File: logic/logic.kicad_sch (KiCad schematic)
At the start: 32 parts, among them J1 DIN41612_03x32_ABC, J2 Conn_02x05_Odd_Even, J3 Conn_02x05_Odd_Even, J5 Conn_02x02_Odd_Even, U1 TPIC6595, U11 LM7805_TO220, U2 TPIC6595, U3 TPIC6595, U4 TPIC6595, U5 TPIC6595, U6 TPIC6595, U7 TPIC6595, U8 TPIC6595, U9 74HC14

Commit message: Commit older work
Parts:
- removed J5: Conn_02x02_Odd_Even, symbol Connector_Generic:Conn_02x02_Odd_Even
- added J4: Conn_02x05_Odd_Even, Connector_PinHeader_2.54mm:PinHeader_2x05_P2.54mm_Vertical, symbol Connector_Generic:Conn_02x05_Odd_Even
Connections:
- net GND: now also J4.1 (Pin_1), J4.3 (Pin_3), J4.5 (Pin_5), J4.7 (Pin_7), J4.9 (Pin_9)
- net at C12.1, U11.1 (VI): now also J4.10 (Pin_10), J4.2 (Pin_2), J4.4 (Pin_4), J4.6 (Pin_6), J4.8 (Pin_8)
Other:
- note added: "J4 UNREG 6.5 - 9V IN"
- note removed: "J5-2, J5-4 UNREG 9V IN"

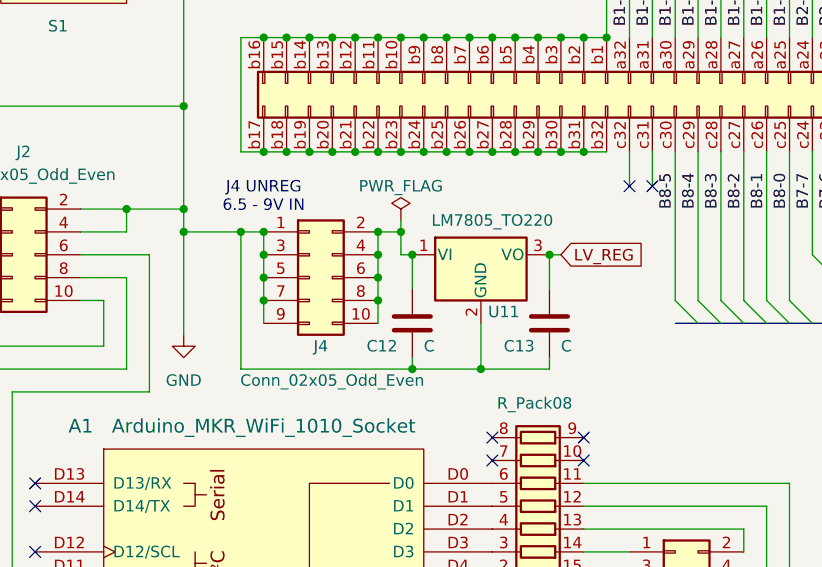
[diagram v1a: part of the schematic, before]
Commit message: Update libraries, schematic, and layout with buck converter
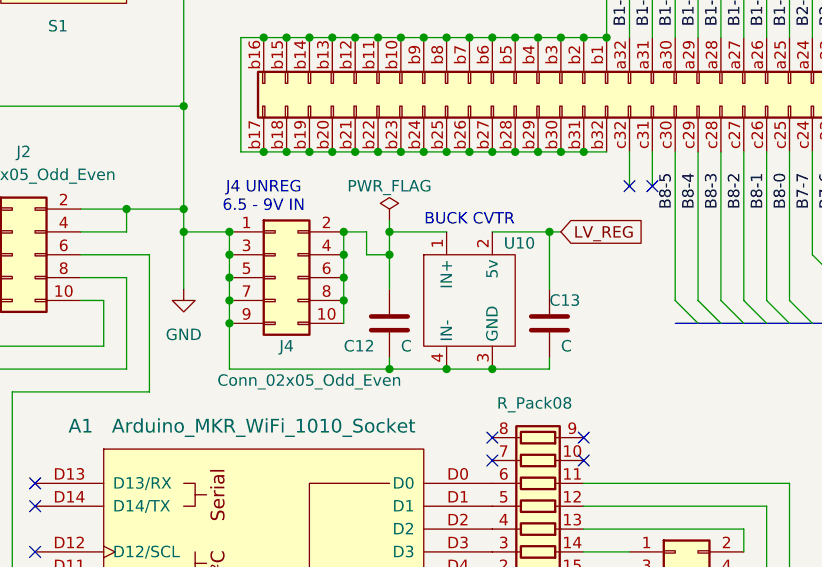
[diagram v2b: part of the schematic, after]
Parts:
- removed U11: LM7805_TO220, Package_TO_SOT_THT:TO-220-3_Vertical, symbol Regulator_Linear:LM7805_TO220
- added U10: ~, NixComp:TR4R7, symbol NixComp:TR4R7
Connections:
- net GND: now also U10.3 (GND), U10.4 (IN-)
- net LV_REG: now also U10.2 (5v)
- net at C12.1, J4.10 (Pin_10), J4.2 (Pin_2)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: now also U10.1 (IN+)
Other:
- note added: "BUCK CVTR"
- moved on the sheet: C12, J4

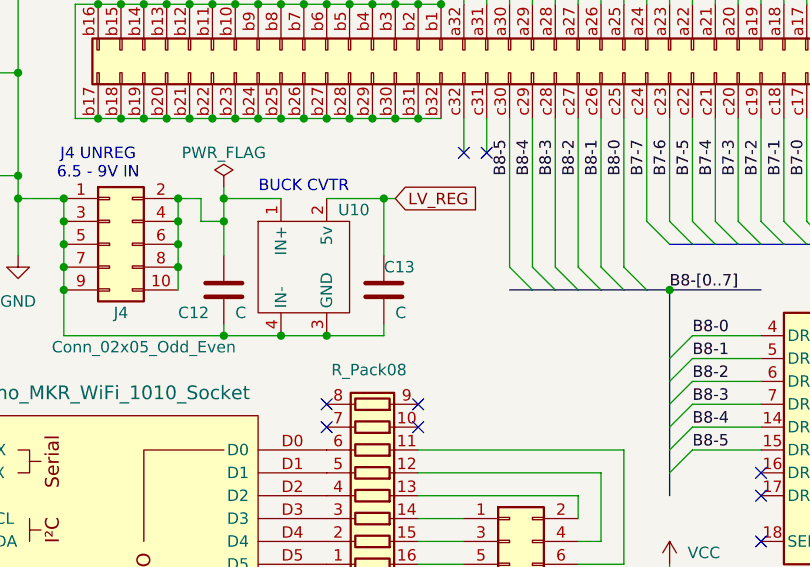
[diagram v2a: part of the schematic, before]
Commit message: Ongoing development of prototype, symbols, footprints, and logic schematic
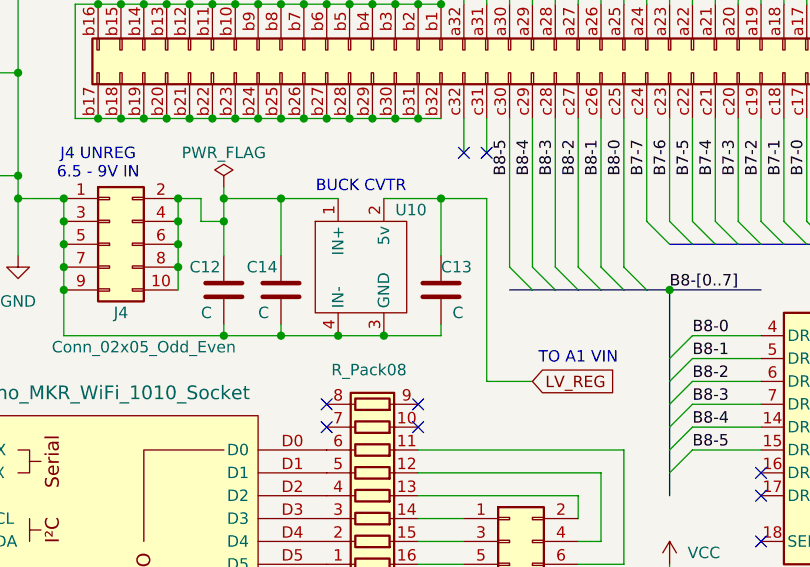
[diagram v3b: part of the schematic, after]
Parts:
- added C14: C, Capacitor_THT:C_Disc_D3.4mm_W2.1mm_P2.50mm, symbol Device:C
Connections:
- net GND: now also C14.2
- net at C12.1, J4.10 (Pin_10), J4.2 (Pin_2)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: now also C14.1
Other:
- note added: "TO A1 VIN"
- moved on the sheet: C13, U10

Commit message: Begin incorporating feedback from prototype. Checkpoint.
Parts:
- removed C1, C10, C12, C13, C14, C2, C3, C4, C5, C6, C7, C8, C9: C, Capacitor_THT:C_Disc_D3.4mm_W2.1mm_P2.50mm, symbol Device:C
- removed C11: C, Capacitor_THT:CP_Radial_D8.0mm_P2.50mm, symbol Device:C
- removed J4: Conn_02x05_Odd_Even, Connector_PinHeader_2.54mm:PinHeader_2x05_P2.54mm_Vertical, symbol Connector_Generic:Conn_02x05_Odd_Even
- removed R1: R, Resistor_THT:R_Axial_DIN0207_L6.3mm_D2.5mm_P10.16mm_Horizontal, symbol Device:R
- removed S1: ~, NixComp:NCH8200HV, symbol NixComp:NCH8200HV_170v
- removed U10: ~, NixComp:TR4R7, symbol NixComp:TR4R7
- removed U9: 74HC14, Package_DIP:DIP-14_W7.62mm_Socket, symbol 74xx:74HC14
- added U9: 74LS244, symbol 74xx:74LS244
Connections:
- net B1-0: no longer J1.a32 (Pin_a32)
- net B1-1: no longer J1.a31 (Pin_a31)
- net B1-2: no longer J1.a30 (Pin_a30)
- net B1-3: no longer J1.a29 (Pin_a29)
- net B1-4: no longer J1.a28 (Pin_a28)
- net B1-5: no longer J1.a27 (Pin_a27)
- net B1-6: no longer J1.a26 (Pin_a26)
- net B1-7: no longer J1.a25 (Pin_a25)
- net B2-0: no longer J1.a24 (Pin_a24)
- net B2-1: no longer J1.a23 (Pin_a23)
- net B2-2: no longer J1.a22 (Pin_a22)
- net B2-3: no longer J1.a21 (Pin_a21)
- net B2-4: no longer J1.a20 (Pin_a20)
- net B2-5: no longer J1.a19 (Pin_a19)
- net B2-6: no longer J1.a18 (Pin_a18)
- net B2-7: no longer J1.a17 (Pin_a17)
- net B3-0: no longer J1.a16 (Pin_a16)
- net B3-1: no longer J1.a15 (Pin_a15)
- net B3-2: no longer J1.a14 (Pin_a14)
- net B3-3: no longer J1.a13 (Pin_a13)
- net B3-4: no longer J1.a12 (Pin_a12)
- net B3-5: no longer J1.a11 (Pin_a11)
- net B3-6: no longer J1.a10 (Pin_a10)
- net B3-7: no longer J1.a9 (Pin_a9)
- net B4-0: no longer J1.a8 (Pin_a8)
- net B4-1: no longer J1.a7 (Pin_a7)
- net B4-2: no longer J1.a6 (Pin_a6)
- net B4-3: no longer J1.a5 (Pin_a5)
- net B4-4: no longer J1.a4 (Pin_a4)
- net B4-5: no longer J1.a3 (Pin_a3)
- net B5-0: no longer J1.c1 (Pin_c1)
- net B5-1: no longer J1.c2 (Pin_c2)
- net B5-2: no longer J1.c3 (Pin_c3)
- net B5-3: no longer J1.c4 (Pin_c4)
- net B5-4: no longer J1.c5 (Pin_c5)
- net B5-5: no longer J1.c6 (Pin_c6)
- net B5-6: no longer J1.c7 (Pin_c7)
- net B5-7: no longer J1.c8 (Pin_c8)
- net B6-0: no longer J1.c9 (Pin_c9)
- net B6-1: no longer J1.c10 (Pin_c10)
- net B6-2: no longer J1.c11 (Pin_c11)
- net B6-3: no longer J1.c12 (Pin_c12)
- net B6-4: no longer J1.c13 (Pin_c13)
- net B6-5: no longer J1.c14 (Pin_c14)
- net B6-6: no longer J1.c15 (Pin_c15)
- net B6-7: no longer J1.c16 (Pin_c16)
- net B7-0: no longer J1.c17 (Pin_c17)
- net B7-1: no longer J1.c18 (Pin_c18)
- net B7-2: no longer J1.c19 (Pin_c19)
- net B7-3: no longer J1.c20 (Pin_c20)
- net B7-4: no longer J1.c21 (Pin_c21)
- net B7-5: no longer J1.c22 (Pin_c22)
- net B7-6: no longer J1.c23 (Pin_c23)
- net B7-7: no longer J1.c24 (Pin_c24)
- net B8-0: no longer J1.c25 (Pin_c25)
- net B8-1: no longer J1.c26 (Pin_c26)
- net B8-2: no longer J1.c27 (Pin_c27)
- net B8-3: no longer J1.c28 (Pin_c28)
- net B8-4: no longer J1.c29 (Pin_c29)
- net B8-5: no longer J1.c30 (Pin_c30)
- net GND: no longer A1.GND, J3.7 (Pin_7), J3.9 (Pin_9)
- net HV_REG: now reaches J1.b1 (Pin_b1), J1.b10 (Pin_b10), J1.b11 (Pin_b11), J1.b12 (Pin_b12), J1.b13 (Pin_b13), J1.b14 (Pin_b14), J1.b15 (Pin_b15), J1.b16 (Pin_b16), J1.b17 (Pin_b17), J1.b18 (Pin_b18), J1.b19 (Pin_b19), J1.b2 (Pin_b2), J1.b20 (Pin_b20), J1.b21 (Pin_b21), J1.b22 (Pin_b22), J1.b23 (Pin_b23), J1.b24 (Pin_b24), J1.b25 (Pin_b25), J1.b26 (Pin_b26), J1.b27 (Pin_b27), J1.b28 (Pin_b28), J1.b29 (Pin_b29), J1.b3 (Pin_b3), J1.b30 (Pin_b30), J1.b31 (Pin_b31), J1.b32 (Pin_b32), J1.b4 (Pin_b4), J1.b5 (Pin_b5), J1.b6 (Pin_b6), J1.b7 (Pin_b7), J1.b8 (Pin_b8), J1.b9 (Pin_b9)
- new net: A1.GND, J3.7 (Pin_7), J3.9 (Pin_9)
- no-connect marks 26 -> 23
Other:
- added sheet Logic-overflow (Logic-overflow.kicad_sch)
- note removed: "BUCK CVTR"
- note removed: "DECOUPLING"
- note removed: "J4 UNREG 6.5 - 9V IN"
- note removed: "NCH8200HV 5VDC 170V"
- note removed: "UNUSED GATES"
- moved on the sheet: J1

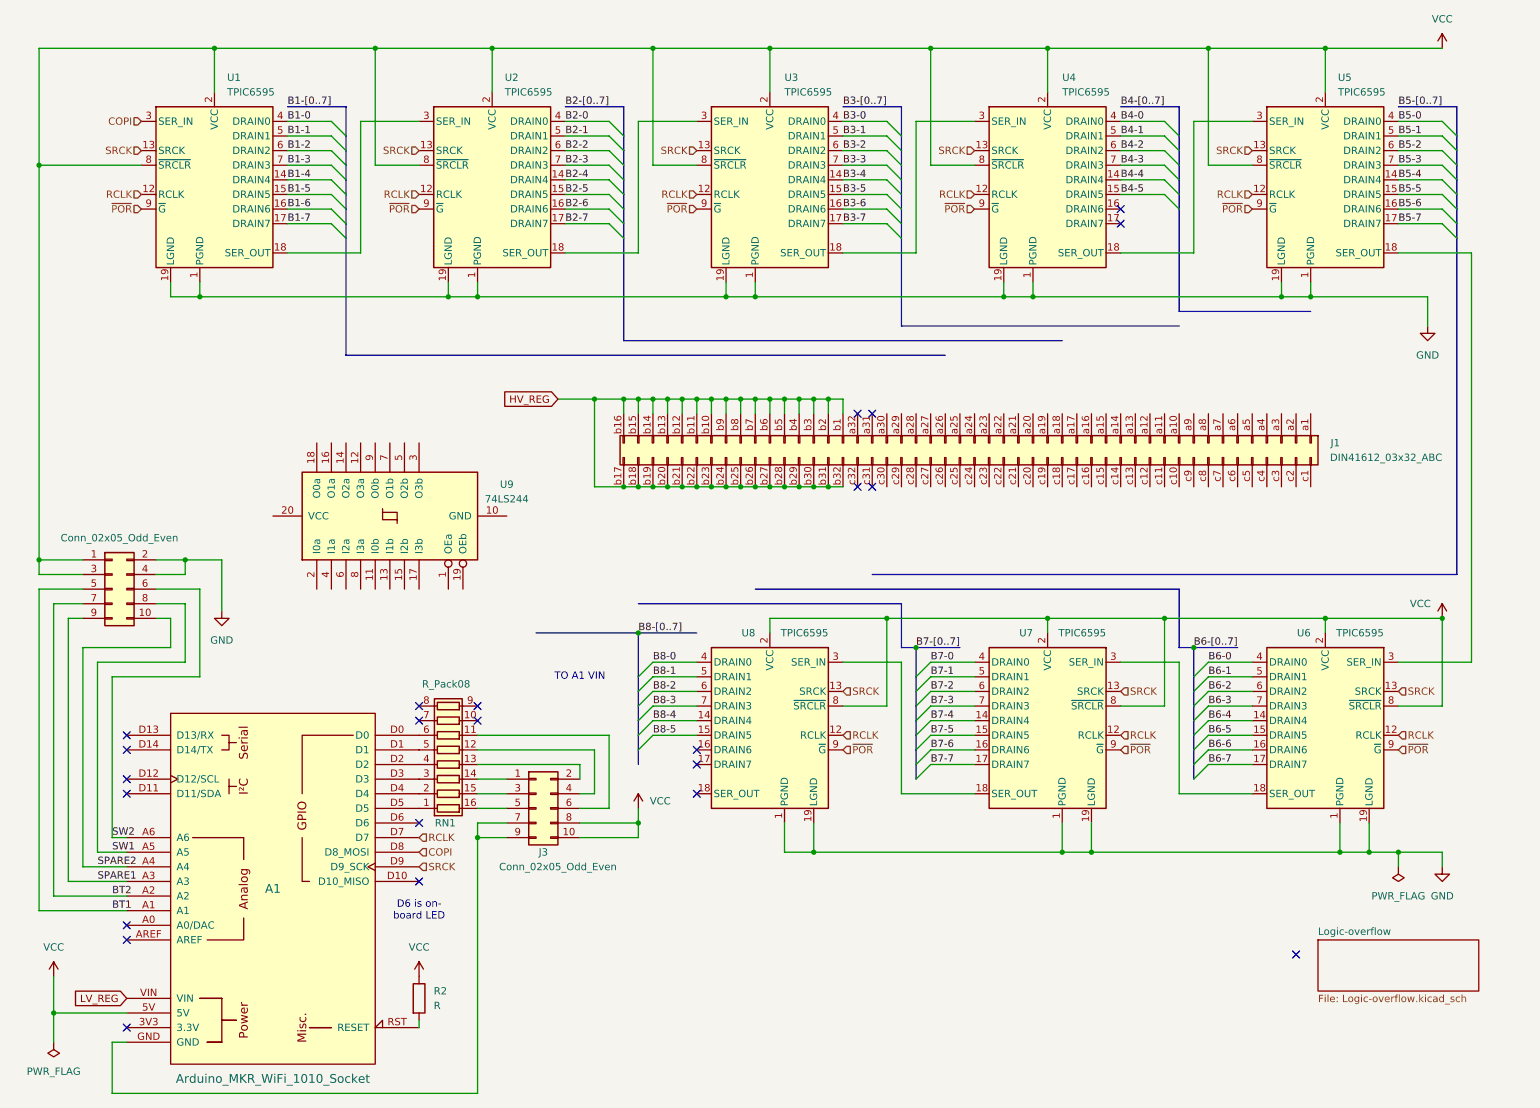
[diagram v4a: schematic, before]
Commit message: Complete schematic and begin logic board layout.
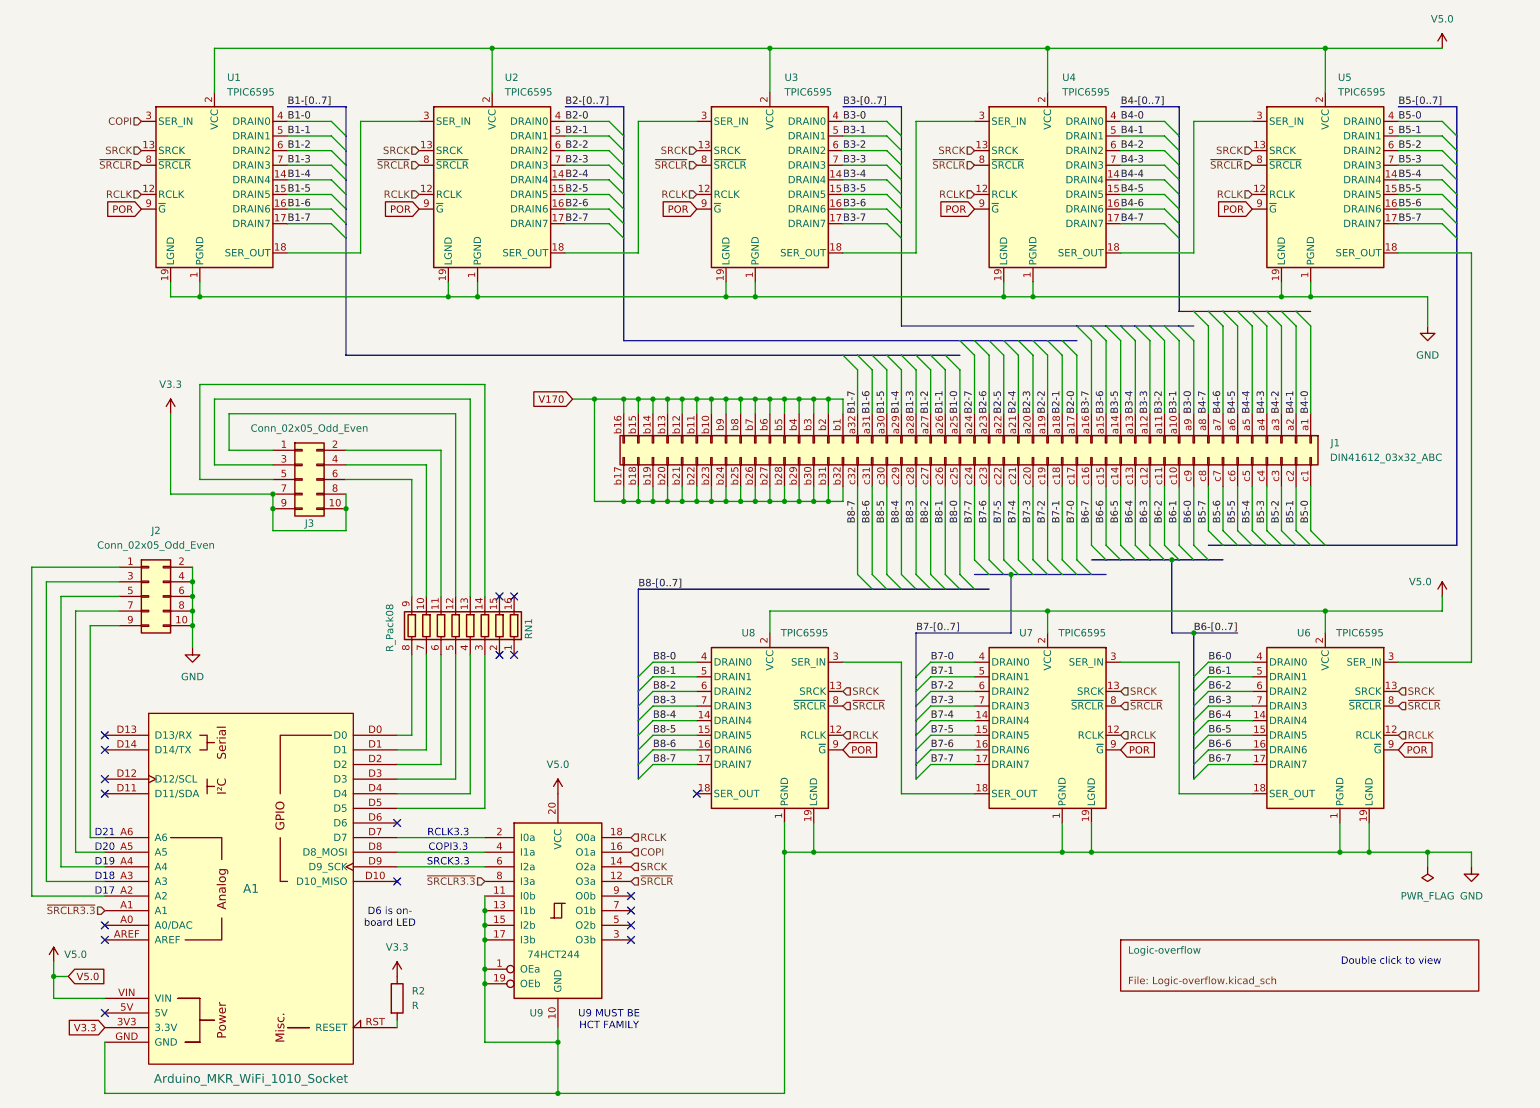
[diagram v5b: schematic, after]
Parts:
- U9: value 74LS244 -> 74HCT244; footprint (none) -> Package_DIP:DIP-20_W7.62mm_Socket_LongPads
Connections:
- net LV_REG is gone; now on net V5.0: A1.VIN
- net B1-0: now also J1.a25 (Pin_a25)
- net B1-1: now also J1.a26 (Pin_a26)
- net B1-2: now also J1.a27 (Pin_a27)
- net B1-3: now also J1.a28 (Pin_a28)
- net B1-4: now also J1.a29 (Pin_a29)
- net B1-5: now also J1.a30 (Pin_a30)
- net B1-6: now also J1.a31 (Pin_a31)
- net B1-7: now also J1.a32 (Pin_a32)
- net B2-0: now also J1.a17 (Pin_a17)
- net B2-1: now also J1.a18 (Pin_a18)
- net B2-2: now also J1.a19 (Pin_a19)
- net B2-3: now also J1.a20 (Pin_a20)
- net B2-4: now also J1.a21 (Pin_a21)
- net B2-5: now also J1.a22 (Pin_a22)
- net B2-6: now also J1.a23 (Pin_a23)
- net B2-7: now also J1.a24 (Pin_a24)
- net B3-0: now also J1.a9 (Pin_a9)
- net B3-1: now also J1.a10 (Pin_a10)
- net B3-2: now also J1.a11 (Pin_a11)
- net B3-3: now also J1.a12 (Pin_a12)
- net B3-4: now also J1.a13 (Pin_a13)
- net B3-5: now also J1.a14 (Pin_a14)
- net B3-6: now also J1.a15 (Pin_a15)
- net B3-7: now also J1.a16 (Pin_a16)
- net B4-0: now also J1.a1 (Pin_a1)
- net B4-1: now also J1.a2 (Pin_a2)
- net B4-2: now also J1.a3 (Pin_a3)
- net B4-3: now also J1.a4 (Pin_a4)
- net B4-4: now also J1.a5 (Pin_a5)
- net B4-5: now also J1.a6 (Pin_a6)
- net B5-0: now also J1.c1 (Pin_c1)
- net B5-1: now also J1.c2 (Pin_c2)
- net B5-2: now also J1.c3 (Pin_c3)
- net B5-3: now also J1.c4 (Pin_c4)
- net B5-4: now also J1.c5 (Pin_c5)
- net B5-5: now also J1.c6 (Pin_c6)
- net B5-6: now also J1.c7 (Pin_c7)
- net B5-7: now also J1.c8 (Pin_c8)
- net B6-0: now also J1.c9 (Pin_c9)
- net B6-1: now also J1.c10 (Pin_c10)
- net B6-2: now also J1.c11 (Pin_c11)
- net B6-3: now also J1.c12 (Pin_c12)
- net B6-4: now also J1.c13 (Pin_c13)
- net B6-5: now also J1.c14 (Pin_c14)
- net B6-6: now also J1.c15 (Pin_c15)
- net B6-7: now also J1.c16 (Pin_c16)
- net B7-0: now also J1.c17 (Pin_c17)
- net B7-1: now also J1.c18 (Pin_c18)
- net B7-2: now also J1.c19 (Pin_c19)
- net B7-3: now also J1.c20 (Pin_c20)
- net B7-4: now also J1.c21 (Pin_c21)
- net B7-5: now also J1.c22 (Pin_c22)
- net B7-6: now also J1.c23 (Pin_c23)
- net B7-7: now also J1.c24 (Pin_c24)
- net B8-0: now also J1.c25 (Pin_c25)
- net B8-1: now also J1.c26 (Pin_c26)
- net B8-2: now also J1.c27 (Pin_c27)
- net B8-3: now also J1.c28 (Pin_c28)
- net B8-4: now also J1.c29 (Pin_c29)
- net B8-5: now also J1.c30 (Pin_c30)
- net COPI: now also U9.16 (O1a); no longer A1.D8 (D8_MOSI)
- net GND: now also A1.GND, J2.10 (Pin_10), J2.6 (Pin_6), J2.8 (Pin_8), U9.1 (OEa), U9.10 (GND), U9.11 (I0b), U9.13 (I1b), U9.15 (I2b), U9.17 (I3b), U9.19 (OEb)
- net RCLK: now also U9.18 (O0a); no longer A1.D7
- net SRCK: now also U9.14 (O2a); no longer A1.D9 (D9_SCK)
- net at J3.1 (Pin_1): now also RN1.12 (R5.2); no longer RN1.14 (R3.2)
- net at J3.2 (Pin_2): now also RN1.11 (R6.2); no longer RN1.13 (R4.2)
- net at J3.3 (Pin_3): now also RN1.13 (R4.2); no longer RN1.15 (R2.2)
- net at J3.4 (Pin_4): now also RN1.10 (R7.2); no longer RN1.12 (R5.2)
- net at J3.5 (Pin_5): now also RN1.14 (R3.2); no longer RN1.16 (R1.2)
- net at J3.6 (Pin_6): now also RN1.9 (R8.2); no longer RN1.11 (R6.2)
- net V3.3: now reaches J3.7 (Pin_7), J3.9 (Pin_9)
- net V3.3: now also A1.3V3 (3.3V), J3.10 (Pin_10), J3.8 (Pin_8), R2.1; no longer A1.GND
- net B8-6: now reaches U8.16 (DRAIN6)
- net B8-6: now also J1.c31 (Pin_c31)
- net B8-7: now reaches U8.17 (DRAIN7)
- net B8-7: now also J1.c32 (Pin_c32)
- net at A1.D0: now also RN1.8 (R8.1); no longer RN1.6 (R6.1)
- net at A1.D1: now also RN1.7 (R7.1); no longer RN1.5 (R5.1)
- net at A1.D2: now also RN1.6 (R6.1); no longer RN1.4 (R4.1)
- net at A1.D3: now also RN1.5 (R5.1); no longer RN1.3 (R3.1)
- net at A1.D4: now also RN1.4 (R4.1); no longer RN1.2 (R2.1)
- net at A1.D5: now also RN1.3 (R3.1); no longer RN1.1 (R1.1)
- net B4-6: now reaches U4.16 (DRAIN6)
- net B4-6: now also J1.a7 (Pin_a7)
- net B4-7: now reaches U4.17 (DRAIN7)
- net B4-7: now also J1.a8 (Pin_a8)
- net ~{SRCLR}: now reaches U9.12 (O3a)
- net ~{SRCLR}: now also U1.8 (~{SRCLR}), U2.8 (~{SRCLR}), U3.8 (~{SRCLR}), U4.8 (~{SRCLR}), U5.8 (~{SRCLR}), U6.8 (~{SRCLR}), U7.8 (~{SRCLR}), U8.8 (~{SRCLR})
- net at U9.2 (I0a): now also A1.D7
- net V5.0: now reaches U9.20 (VCC)
- net V5.0: now also U1.2 (VCC), U2.2 (VCC), U3.2 (VCC), U4.2 (VCC), U5.2 (VCC), U6.2 (VCC), U7.2 (VCC), U8.2 (VCC)
- net at U9.4 (I1a): now also A1.D8 (D8_MOSI)
- net at U9.6 (I2a): now also A1.D9 (D9_SCK)
- net ~{SRCLR3.3}: now reaches U9.8 (I3a)
- net ~{SRCLR3.3}: now also A1.A1
- net BT1: no longer names the net of J2.5 (Pin_5)
- net BT1: now also A1.A4; no longer A1.A1
- net BT2: no longer names the net of A1.A2
- net BT2: now also J2.1 (Pin_1); no longer J2.7 (Pin_7)
- net HV_REG renamed V170
- net SPARE1: no longer names the net of A1.A3
- net SPARE1: now also J2.3 (Pin_3); no longer J2.9 (Pin_9)
- removed net SPARE2: A1.A4, J2.10 (Pin_10)
- net SW1: no longer names the net of A1.A5
- net SW1: now also J2.7 (Pin_7); no longer J2.8 (Pin_8)
- net SW2: no longer names the net of A1.A6
- net SW2: now also J2.9 (Pin_9); no longer J2.6 (Pin_6)
- removed net VCC: A1.5V, J2.1 (Pin_1), J2.3 (Pin_3), J3.10 (Pin_10), J3.8 (Pin_8), R2.1, U1.2 (VCC), U1.8 (~{SRCLR}), U2.2 (VCC), U2.8 (~{SRCLR}), U3.2 (VCC), U3.8 (~{SRCLR}), U4.2 (VCC), U4.8 (~{SRCLR}), U5.2 (VCC), U5.8 (~{SRCLR}), U6.2 (VCC), U6.8 (~{SRCLR}), U7.2 (VCC), U7.8 (~{SRCLR}), U8.2 (VCC), U8.8 (~{SRCLR})
- net ~{POR} renamed POR
- no-connect marks 23 -> 18
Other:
- note added: "COPI3.3"
- note added: "D17"
- note added: "D18"
- note added: "D19"
- note added: "D20"
- note added: "D21"
- note added: "Double click to view"
- note added: "RCLK3.3"
- note added: "SRCK3.3"
- note added: "U9 MUST BE HCT FAMILY"
- note removed: "TO A1 VIN"
- moved on the sheet: A1, J3, R2, U9
